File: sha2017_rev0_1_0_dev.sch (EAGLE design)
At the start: 196 parts, among them IC1 CP210X_USB_UART, IC2 AP7215, IC3 ESP32WROOM32, IC4 MCP73833, IC5 FXL6408, IC6 CPT112, Q1 MOSFET-PCHANNEL, Q2 MMBT2222A, Q3 MMBT2222A, Q4 MMBT2222A, Q5 MMBT2222A, Q6 SI1304 BDL, Q7 MMBT2222A, Q8 MOSFET-PCHANNEL, T1 SI2301DS, X1 2908-05WB-MG, X3 JST-PH3

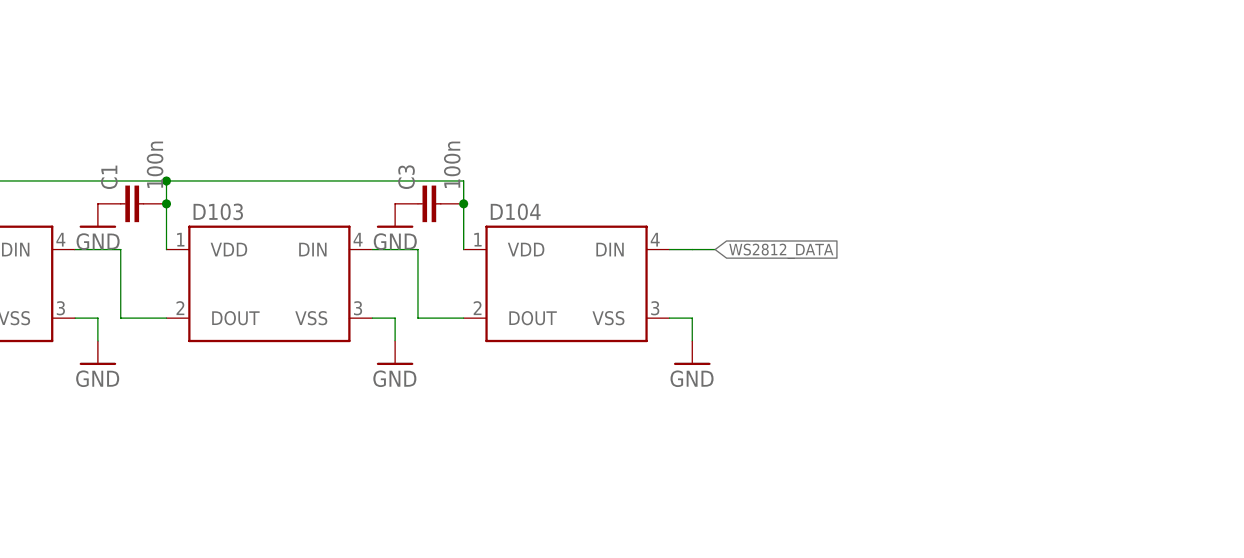
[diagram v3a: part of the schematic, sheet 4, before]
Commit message: add 1 LED
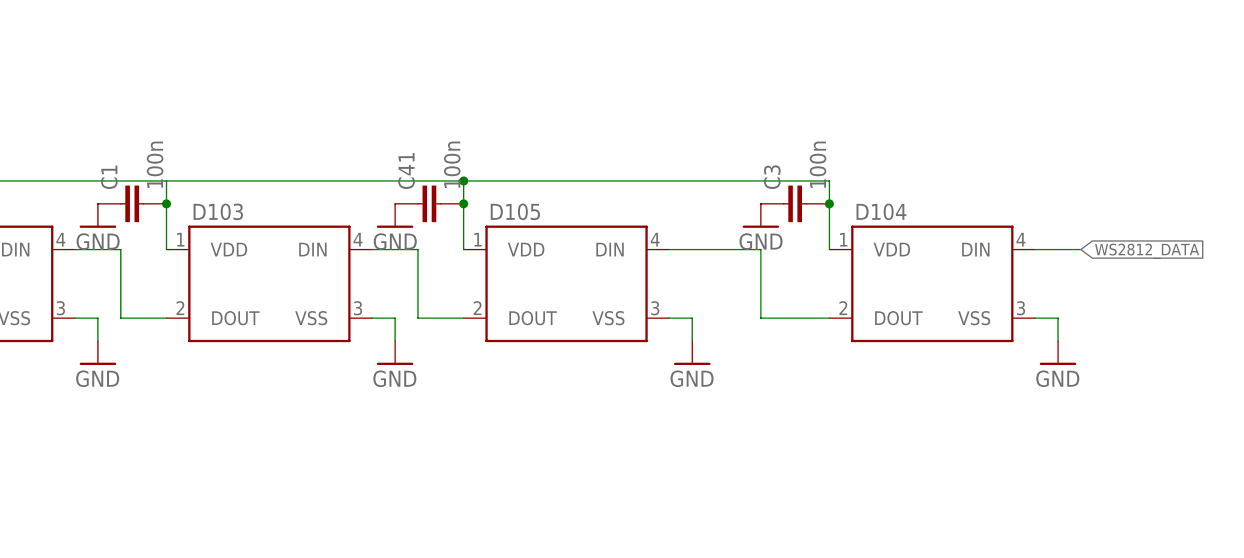
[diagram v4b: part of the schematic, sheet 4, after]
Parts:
- added C41: 100n, sha2017_rev0_1_0_dev:C0603-DASHES
- added D105: (no value), SparkFun-LED:WS2812B
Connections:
- removed net N$51: D103.DIN, D104.DOUT
- new net N$3: D103.DIN, D105.DOUT
- new net N$4: D104.DOUT, D105.DIN
- net GND: now also C41.1, D105.VSS
- net WS2812_POWER: now also C41.2, D105.VDD
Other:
- moved on the sheet: C3, D104
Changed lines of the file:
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@@
 <attribute name="PARTNO" value="NAP"/>
 </part>
+<part name="D105" library="SparkFun-LED" deviceset="WS2812B" device="">
+<attribute name="PARTNO" value="WS2812B"/>
+</part>
+<part name="GND90" library="supply1" deviceset="GND" device=""/>
+<part name="C41" library="sha2017_rev0_1_0_dev" deviceset="C0603-DASHES" device="" value="100n">
+<attribute name="PARTNO" value="GRM188R71H104KA93D"/>
+</part>
+<part name="GND93" library="supply1" deviceset="GND" device=""/>
 </parts>
 <sheets>
@@
 <attribute name="PARTNO" x="213.36" y="91.44" size="5.08" layer="96" display="off"/>
 </instance>
-<instance part="D104" gate="G$1" x="246.38" y="91.44">
-<attribute name="PARTNO" x="246.38" y="91.44" size="5.08" layer="96" display="off"/>
+<instance part="D104" gate="G$1" x="287.02" y="91.44">
+<attribute name="PARTNO" x="287.02" y="91.44" size="5.08" layer="96" display="off"/>
 </instance>
 <instance part="GND4" gate="1" x="134.62" y="83.82"/>
@@
 <instance part="GND23" gate="1" x="200.66" y="83.82"/>
 <instance part="GND30" gate="1" x="233.68" y="83.82"/>
-<instance part="GND38" gate="1" x="266.7" y="83.82"/>
+<instance part="GND38" gate="1" x="307.34" y="83.82"/>
 <instance part="Q1" gate="G$1" x="81.28" y="88.9"/>
 <instance part="Q2" gate="G$1" x="63.5" y="81.28">
@@
 <attribute name="PARTNO" x="204.47" y="101.6" size="5.08" layer="96" display="off"/>
 </instance>
-<instance part="C3" gate="G$1" x="237.49" y="101.6" rot="R90">
-<attribute name="PARTNO" x="237.49" y="101.6" size="5.08" layer="96" display="off"/>
+<instance part="C3" gate="G$1" x="278.13" y="101.6" rot="R90">
+<attribute name="PARTNO" x="278.13" y="101.6" size="5.08" layer="96" display="off"/>
 </instance>
 <instance part="GND40" gate="1" x="134.62" y="99.06" rot="MR0"/>
 <instance part="GND41" gate="1" x="167.64" y="99.06" rot="MR0"/>
 <instance part="GND42" gate="1" x="200.66" y="99.06" rot="MR0"/>
-<instance part="GND43" gate="1" x="233.68" y="99.06" rot="MR0"/>
+<instance part="GND43" gate="1" x="274.32" y="99.06" rot="MR0"/>
 <instance part="C2" gate="G$1" x="105.41" y="101.6" rot="R90">
 <attribute name="PARTNO" x="105.41" y="101.6" size="5.08" layer="96" display="off"/>
@@
 <instance part="P+6" gate="VCC" x="81.28" y="101.6"/>
 <instance part="FRAME2" gate="G$1" x="0" y="0"/>
+<instance part="D105" gate="G$1" x="246.38" y="91.44">
+<attribute name="PARTNO" x="246.38" y="91.44" size="5.08" layer="96" display="off"/>
+</instance>
+<instance part="GND90" gate="1" x="266.7" y="83.82"/>
+<instance part="C41" gate="G$1" x="237.49" y="101.6" rot="R90">
+<attribute name="PARTNO" x="237.49" y="101.6" size="5.08" layer="96" display="off"/>
+</instance>
+<instance part="GND93" gate="1" x="233.68" y="99.06" rot="MR0"/>
 </instances>
 <busses>
@@
 <segment>
 <pinref part="D104" gate="G$1" pin="VSS"/>
-<wire x1="264.16" y1="88.9" x2="266.7" y2="88.9" width="0.1524" layer="91"/>
-<wire x1="266.7" y1="88.9" x2="266.7" y2="86.36" width="0.1524" layer="91"/>
+<wire x1="304.8" y1="88.9" x2="307.34" y2="88.9" width="0.1524" layer="91"/>
+<wire x1="307.34" y1="88.9" x2="307.34" y2="86.36" width="0.1524" layer="91"/>
 <pinref part="GND38" gate="1" pin="GND"/>
 </segment>
@@
 <pinref part="C4" gate="G$1" pin="2"/>
 <pinref part="GND45" gate="1" pin="GND"/>
+</segment>
+<segment>
+<pinref part="D105" gate="G$1" pin="VSS"/>
+<wire x1="264.16" y1="88.9" x2="266.7" y2="88.9" width="0.1524" layer="91"/>
+<wire x1="266.7" y1="88.9" x2="266.7" y2="86.36" width="0.1524" layer="91"/>
+<pinref part="GND90" gate="1" pin="GND"/>
+</segment>
+<segment>
+<pinref part="C41" gate="G$1" pin="1"/>
+<pinref part="GND93" gate="1" pin="GND"/>
 </segment>
 </net>
@@
 <pinref part="D103" gate="G$1" pin="DOUT"/>
 <wire x1="203.2" y1="88.9" x2="208.28" y2="88.9" width="0.1524" layer="91"/>
-</segment>
-</net>
-<net name="N$51" class="0">
-<segment>
-<pinref part="D103" gate="G$1" pin="DIN"/>
-<wire x1="231.14" y1="96.52" x2="236.22" y2="96.52" width="0.1524" layer="91"/>
-<wire x1="236.22" y1="96.52" x2="236.22" y2="88.9" width="0.1524" layer="91"/>
-<pinref part="D104" gate="G$1" pin="DOUT"/>
-<wire x1="236.22" y1="88.9" x2="241.3" y2="88.9" width="0.1524" layer="91"/>
 </segment>
 </net>
@@
 <net name="WS2812_DATA" class="0">
 <segment>
-<wire x1="269.24" y1="96.52" x2="266.7" y2="96.52" width="0.1524" layer="91"/>
+<wire x1="309.88" y1="96.52" x2="307.34" y2="96.52" width="0.1524" layer="91"/>
 <pinref part="D104" gate="G$1" pin="DIN"/>
-<label x="269.24" y="96.52" size="1.27" layer="95" xref="yes"/>
-<wire x1="266.7" y1="96.52" x2="264.16" y2="96.52" width="0.1524" layer="91"/>
+<label x="309.88" y="96.52" size="1.27" layer="95" xref="yes"/>
+<wire x1="307.34" y1="96.52" x2="304.8" y2="96.52" width="0.1524" layer="91"/>
 </segment>
 </net>
@@
 <wire x1="88.9" y1="81.28" x2="88.9" y2="101.6" width="0.1524" layer="91"/>
 <wire x1="88.9" y1="101.6" x2="88.9" y2="104.14" width="0.1524" layer="91"/>
-<pinref part="D104" gate="G$1" pin="VDD"/>
 <wire x1="88.9" y1="104.14" x2="109.22" y2="104.14" width="0.1524" layer="91"/>
 <wire x1="109.22" y1="104.14" x2="142.24" y2="104.14" width="0.1524" layer="91"/>
 <wire x1="142.24" y1="104.14" x2="175.26" y2="104.14" width="0.1524" layer="91"/>
 <wire x1="175.26" y1="104.14" x2="208.28" y2="104.14" width="0.1524" layer="91"/>
-<wire x1="208.28" y1="104.14" x2="241.3" y2="104.14" width="0.1524" layer="91"/>
-<wire x1="241.3" y1="104.14" x2="241.3" y2="101.6" width="0.1524" layer="91"/>
 <pinref part="D100" gate="G$1" pin="VDD"/>
-<wire x1="241.3" y1="101.6" x2="241.3" y2="96.52" width="0.1524" layer="91"/>
 <wire x1="109.22" y1="104.14" x2="109.22" y2="101.6" width="0.1524" layer="91"/>
 <pinref part="D101" gate="G$1" pin="VDD"/>
@@
 <wire x1="208.28" y1="101.6" x2="208.28" y2="104.14" width="0.1524" layer="91"/>
 <junction x="208.28" y="101.6"/>
-<pinref part="C3" gate="G$1" pin="2"/>
-<junction x="241.3" y="101.6"/>
 <pinref part="C2" gate="G$1" pin="2"/>
 <junction x="109.22" y="101.6"/>
@@
 <junction x="142.24" y="104.14"/>
 <junction x="175.26" y="104.14"/>
-<junction x="208.28" y="104.14"/>
 <pinref part="C4" gate="G$1" pin="1"/>
 <junction x="81.28" y="81.28"/>
 <label x="88.9" y="104.14" size="1.27" layer="95" rot="R90" xref="yes"/>
+<pinref part="C41" gate="G$1" pin="2"/>
+<wire x1="241.3" y1="101.6" x2="241.3" y2="104.14" width="0.1524" layer="91"/>
+<junction x="241.3" y="101.6"/>
+<pinref part="D105" gate="G$1" pin="VDD"/>
+<wire x1="241.3" y1="96.52" x2="241.3" y2="101.6" width="0.1524" layer="91"/>
+<wire x1="208.28" y1="104.14" x2="241.3" y2="104.14" width="0.1524" layer="91"/>
+<pinref part="D104" gate="G$1" pin="VDD"/>
+<wire x1="281.94" y1="104.14" x2="281.94" y2="101.6" width="0.1524" layer="91"/>
+<pinref part="C3" gate="G$1" pin="2"/>
+<junction x="281.94" y="101.6"/>
+<wire x1="281.94" y1="101.6" x2="281.94" y2="96.52" width="0.1524" layer="91"/>
+<wire x1="241.3" y1="104.14" x2="281.94" y2="104.14" width="0.1524" layer="91"/>
+<junction x="241.3" y="104.14"/>
 </segment>
 </net>
@@
 </segment>
 </net>
+<net name="N$3" class="0">
+<segment>
+<wire x1="231.14" y1="96.52" x2="236.22" y2="96.52" width="0.1524" layer="91"/>
+<wire x1="236.22" y1="96.52" x2="236.22" y2="88.9" width="0.1524" layer="91"/>
+<pinref part="D105" gate="G$1" pin="DOUT"/>
+<wire x1="236.22" y1="88.9" x2="241.3" y2="88.9" width="0.1524" layer="91"/>
+<pinref part="D103" gate="G$1" pin="DIN"/>
+</segment>
+</net>
+<net name="N$4" class="0">
+<segment>
+<pinref part="D105" gate="G$1" pin="DIN"/>
+<wire x1="264.16" y1="96.52" x2="274.32" y2="96.52" width="0.1524" layer="91"/>
+<wire x1="274.32" y1="96.52" x2="274.32" y2="88.9" width="0.1524" layer="91"/>
+<pinref part="D104" gate="G$1" pin="DOUT"/>
+<wire x1="274.32" y1="88.9" x2="281.94" y2="88.9" width="0.1524" layer="91"/>
+</segment>
+</net>

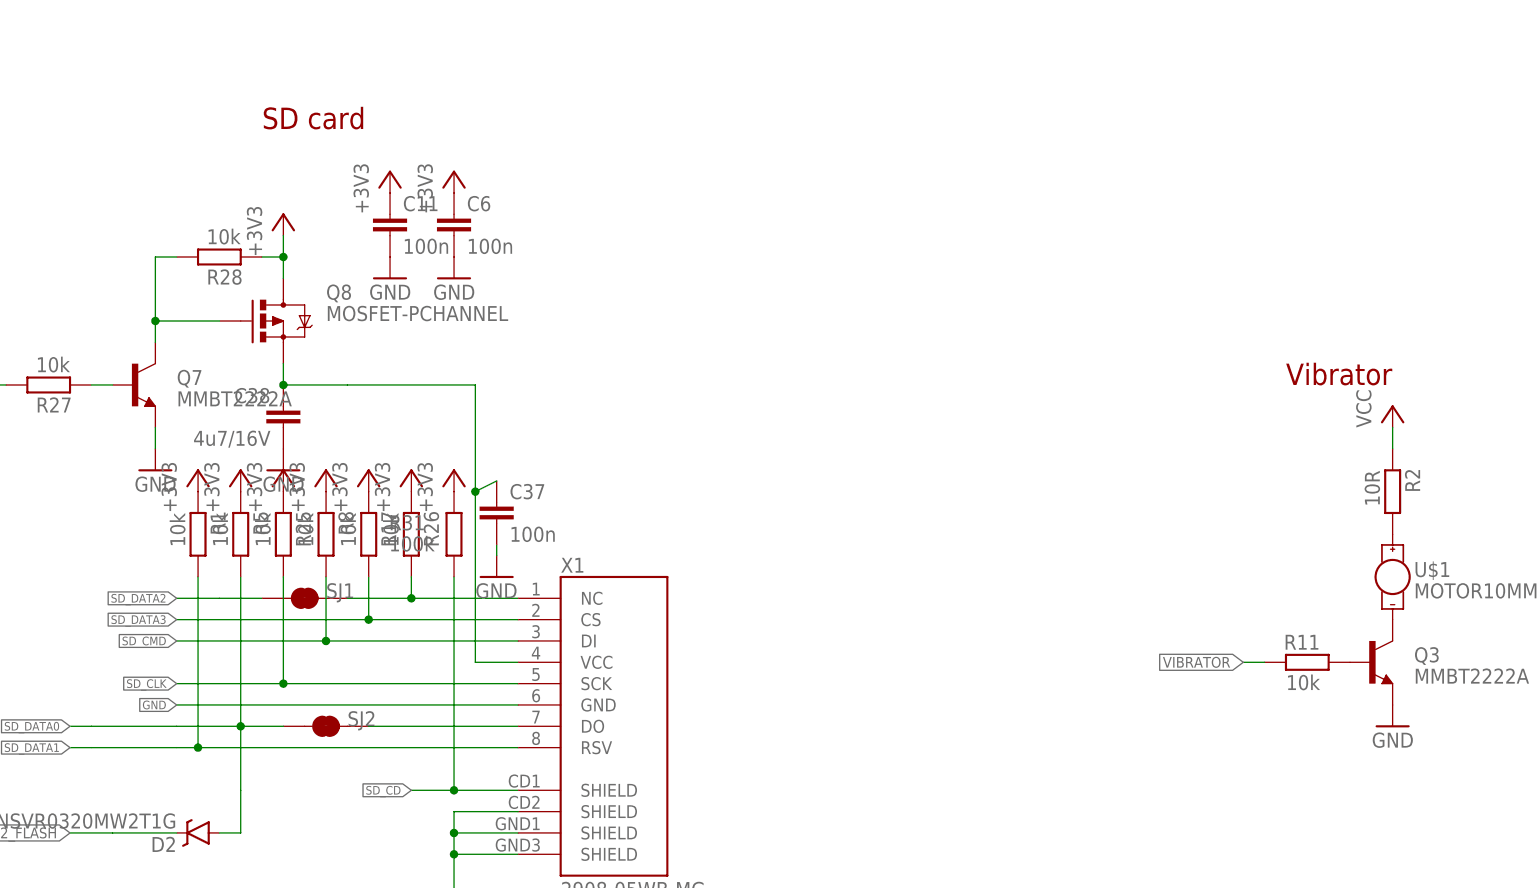
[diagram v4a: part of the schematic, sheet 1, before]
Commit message: adjusted values and add moe coper to the charger region
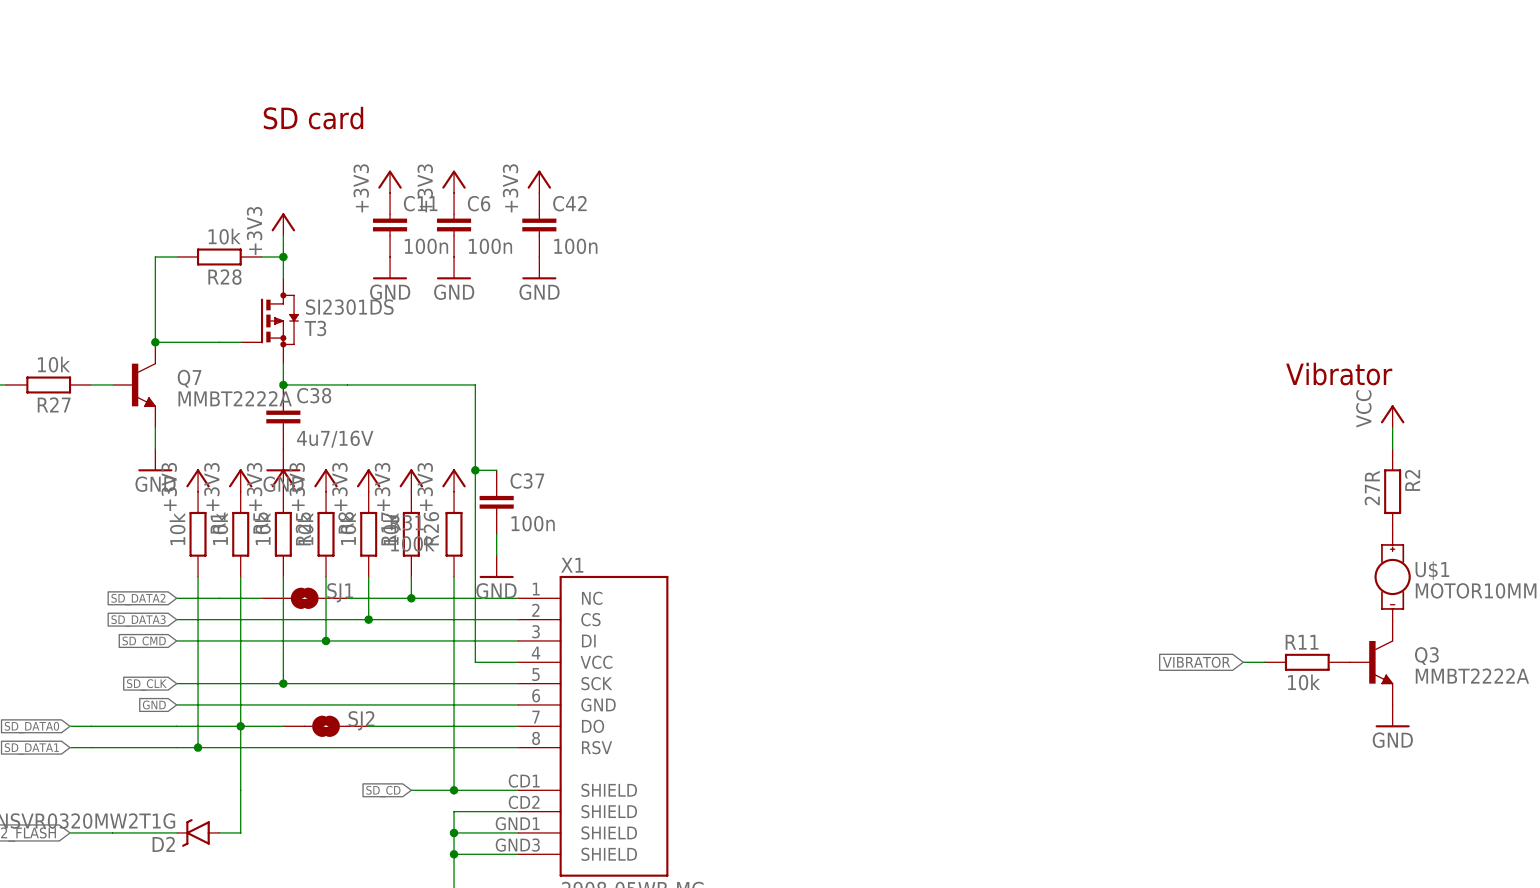
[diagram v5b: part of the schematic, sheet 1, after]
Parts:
- removed Q1, Q8: MOSFET-PCHANNEL, SparkFun-DiscreteSemi:MOSFET-PCHANNEL
- added C42: 100n, sha2017_rev0_1_0_dev:C0603-DASHES
- added T2, T3: SI2301DS, transistor-small-signal:BSS84
- C22, C32: value 10u -> 4u7/16V; device rcl:C-EUC0805K -> rcl:C-EUC0805; PARTNO (none) -> GRM21BR61C475KA88K
- C27, C28: PARTNO (none) -> GRM188R71H104KA93D
- C38, C4: device 00ralf:C0603-DASHES -> rcl:C-EUC0805; PARTNO (none) -> GRM21BR61C475KA88K
- C39: value (none) -> 100n; PARTNO (none) -> GRM188R71H104KA93D
- D1: PARTNO PMEG4005EJ,115 -> SD05-7
- D100, D101, D102, D103, D104, D105: value (none) -> SK6812; PARTNO WS2812B -> SK6812
- R2: value 10R -> 27R
- SJ1, SJ2: value JUMPER-PAD-2-NC_BY_TRACE -> JUMPER-PAD-2-NOYES_SILK; device SparkFun-Passives:JUMPER-PAD-2-NC_BY_TRACE -> SparkFun-Passives:JUMPER-PAD-2-NOYES_SILK; PARTNO (none) -> NAP
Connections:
- net +3V3: now also C42.1; no longer Q8.D
- net +5V: now also C22.1; no longer C22.2
- net 3V3_SWITCHED: no longer Q8.S
- net GND: now also C22.2, C32.2, C42.2; no longer C22.1, C32.1
- net N$17: now also T3.G; no longer Q8.G
- net N$49: now also C32.1; no longer C32.2
- net N$53: now also T2.G; no longer Q1.G
- net VCC: no longer Q1.D
- net WS2812_POWER: no longer Q1.S
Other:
- moved on the sheet: C22, C32, C37
